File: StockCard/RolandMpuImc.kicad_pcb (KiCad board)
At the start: 2 copper layers, 292.1 x 88 mm, 110 parts, among them IC1 LC3517, IC10 74LS138, IC11 74LS573, IC12 74LS86_P, IC13 74LS688, IC14 HEF4093B, IC15 74LS688, IC16 5218, IC2 HG62E08, IC3 HD6801VD855P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

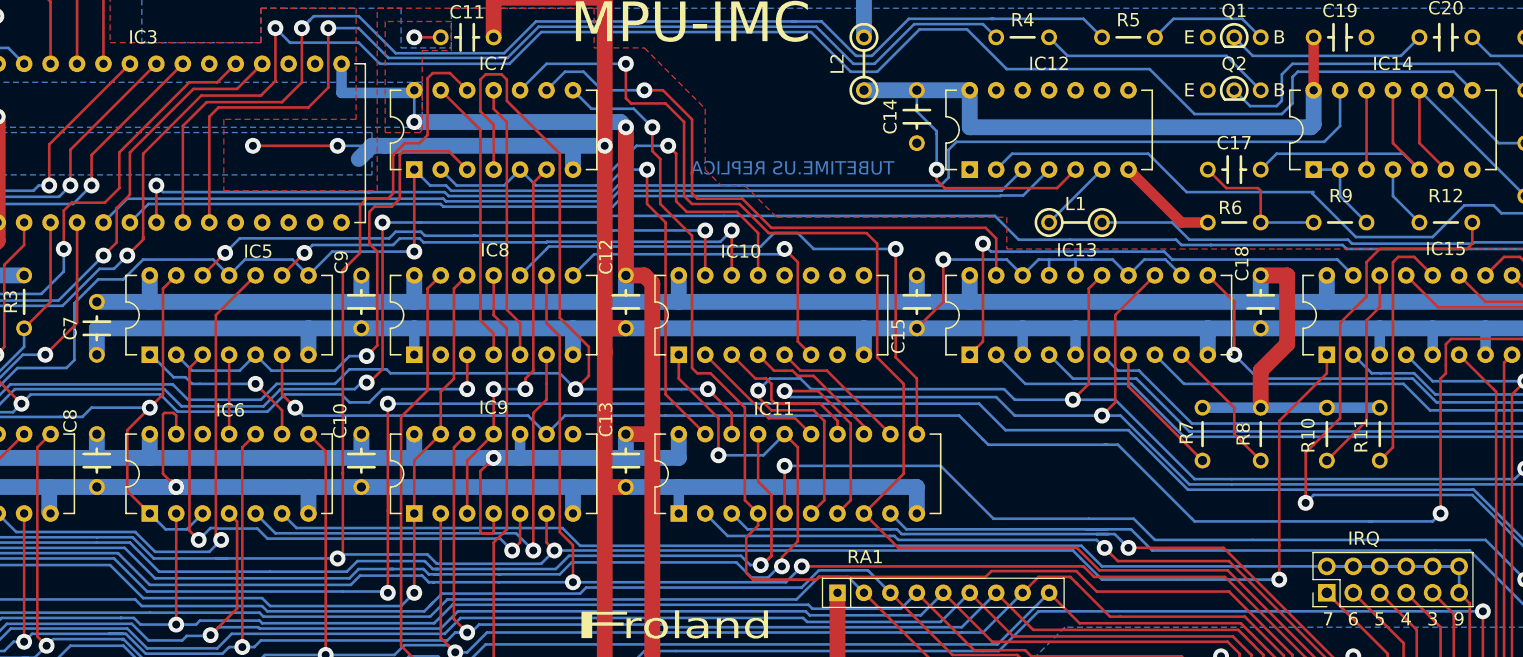
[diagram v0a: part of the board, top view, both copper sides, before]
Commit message: Fix IC3 pin swap and a few part numbers
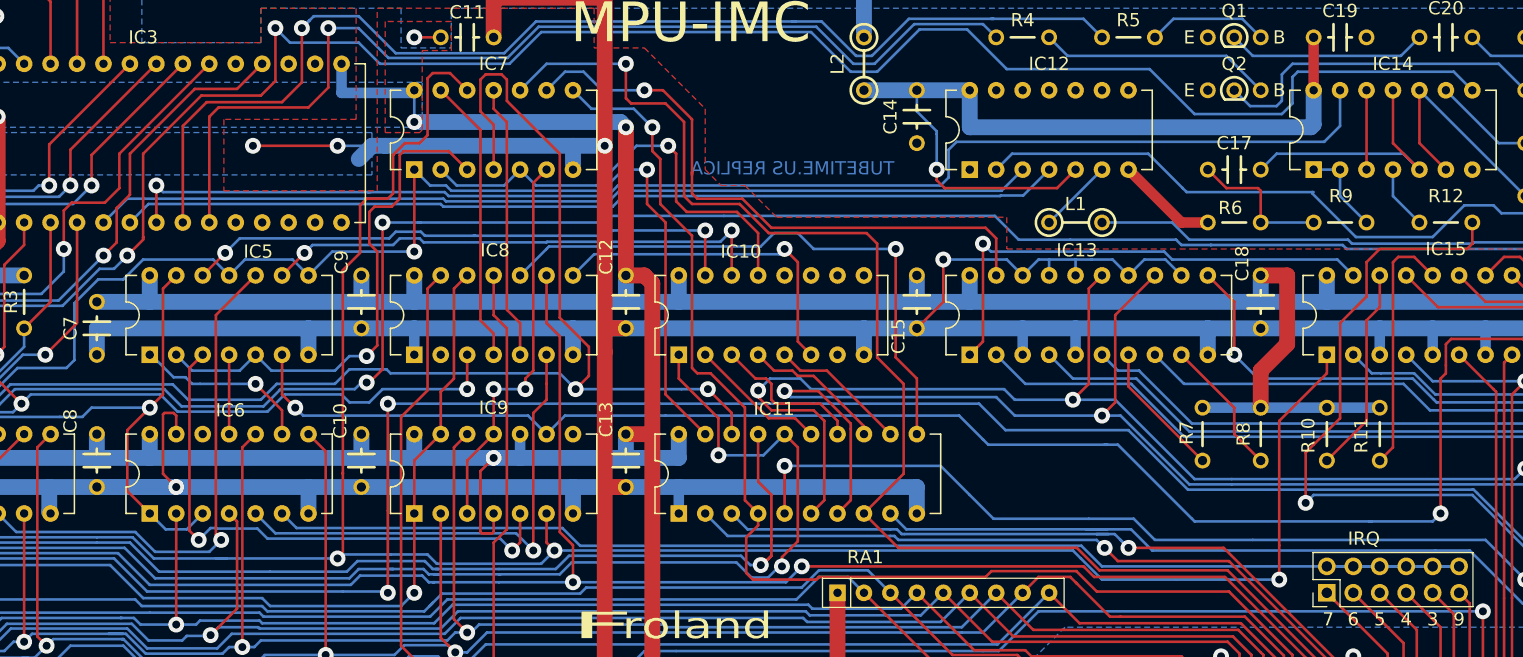
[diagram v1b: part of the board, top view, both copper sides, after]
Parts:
- C5A1, C5B1: value C_Small -> 15p
- IC1: value LC3517 -> LC3517 (or HY6116AP-10)
- IC11: value 74LS573 -> 74ALS573
- RA1: value R_Network08 -> 33K
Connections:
- IC3 pad 25: Net-(IC2-Pad16) -> (no net)
- IC3 pad 26: (no net) -> Net-(IC2-Pad16)
- IC6 pad 6: /IRQ9 -> Net-(IC6-Pad6)
- IRQ1 pad 10: /IRQ9 -> Net-(IC6-Pad6)
- IRQ1 pad 12: /IRQ9 -> Net-(IC6-Pad6)
- IRQ1 pad 2: /IRQ9 -> Net-(IC6-Pad6)
- IRQ1 pad 4: /IRQ9 -> Net-(IC6-Pad6)
- IRQ1 pad 6: /IRQ9 -> Net-(IC6-Pad6)
- IRQ1 pad 8: /IRQ9 -> Net-(IC6-Pad6)
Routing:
- net /IRQ9: track 153.0 -> 20.8 mm
- net Net-(IC6-Pad6): track 0.00 -> 129.6 mm
- net Net-(IC2-Pad16): track 106.8 -> 104.2 mm
